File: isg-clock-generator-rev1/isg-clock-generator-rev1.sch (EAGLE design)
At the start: 160 parts, among them IC1 LMK03318RHSR, IC4 TPS7A8001DRBR, IC5 TPS7A8001DRBR, Q1 7M50072001, X1 OUT2_P, X2 OUT2_N, X3 OUT0_P, X4 PRIREF_P, X5 PRIREF_N, X6 V_IN_EXT

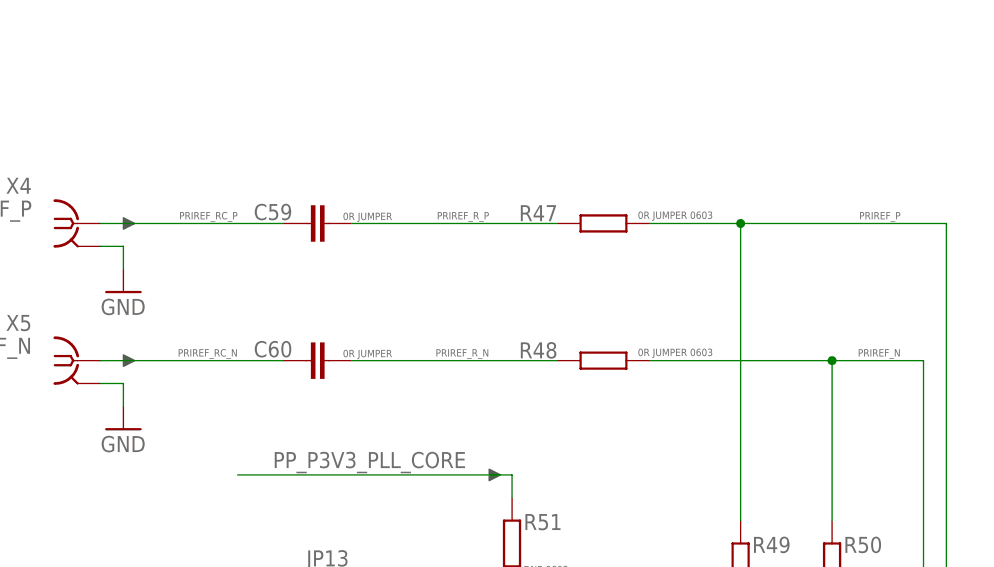
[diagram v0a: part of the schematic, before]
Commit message: Preliminary connections made to PRIREF inputs
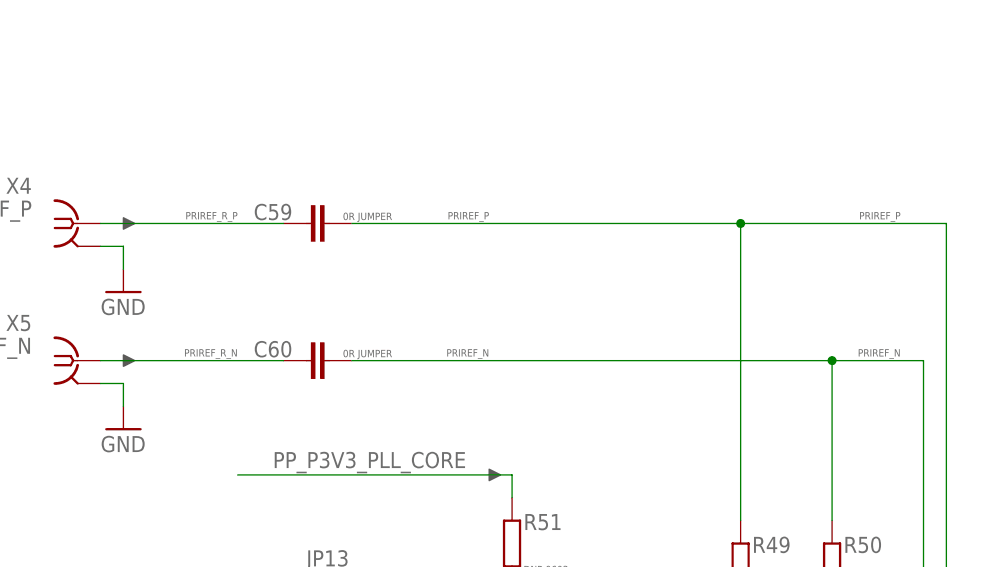
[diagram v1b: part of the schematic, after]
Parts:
- removed R47, R48: 0R JUMPER 0603, rcl-modified-footprints:R-EU_R0603
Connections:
- removed net PRIREF_RC_N: C60.1, X5.1
- removed net PRIREF_RC_P: C59.1, X4.1
- net PRIREF_N: now also C60.2; no longer R48.1
- net PRIREF_P: now also C59.2; no longer R47.1
- net PRIREF_R_N: now also C60.1, X5.1; no longer C60.2, R48.2
- net PRIREF_R_P: now also C59.1, X4.1; no longer C59.2, R47.2
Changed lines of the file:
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@@
 <part name="GND80" library="supply1" library_urn="urn:adsk.eagle:library:371" deviceset="GND" device=""/>
 <part name="GND81" library="supply1" library_urn="urn:adsk.eagle:library:371" deviceset="GND" device=""/>
-<part name="R47" library="rcl-modified-footprints" deviceset="R-EU_" device="R0603" package3d_urn="urn:adsk.eagle:package:23555/2" value="0R JUMPER 0603"/>
-<part name="R48" library="rcl-modified-footprints" deviceset="R-EU_" device="R0603" package3d_urn="urn:adsk.eagle:package:23555/2" value="0R JUMPER 0603"/>
 <part name="C59" library="rcl-modified-footprints" deviceset="C-EU" device="C0603" package3d_urn="urn:adsk.eagle:package:23616/2" value="0R JUMPER"/>
 <part name="C60" library="rcl-modified-footprints" deviceset="C-EU" device="C0603" package3d_urn="urn:adsk.eagle:package:23616/2" value="0R JUMPER"/>
@@
 <attribute name="VALUE" x="43.18" y="231.14" size="1.778" layer="96"/>
 </instance>
-<instance part="R47" gate="G$1" x="99.06" y="256.54" smashed="yes" rot="R180">
-<attribute name="NAME" x="93.98" y="258.572" size="1.778" layer="95" rot="R180"/>
-<attribute name="VALUE" x="102.87" y="257.048" size="0.8128" layer="96"/>
-</instance>
-<instance part="R48" gate="G$1" x="99.06" y="241.3" smashed="yes" rot="R180">
-<attribute name="NAME" x="93.98" y="243.332" size="1.778" layer="95" rot="R180"/>
-<attribute name="VALUE" x="102.87" y="241.808" size="0.8128" layer="96"/>
-</instance>
 <instance part="C59" gate="G$1" x="66.04" y="256.54" smashed="yes" rot="R90">
 <attribute name="NAME" x="64.516" y="258.699" size="1.778" layer="95" rot="R180"/>
@@
 <wire x1="134.62" y1="165.1" x2="134.62" y2="241.3" width="0.1524" layer="91"/>
 <wire x1="134.62" y1="241.3" x2="124.46" y2="241.3" width="0.1524" layer="91"/>
-<pinref part="R48" gate="G$1" pin="1"/>
 <pinref part="R50" gate="G$1" pin="2"/>
-<wire x1="124.46" y1="241.3" x2="104.14" y2="241.3" width="0.1524" layer="91"/>
 <wire x1="124.46" y1="223.52" x2="124.46" y2="241.3" width="0.1524" layer="91"/>
 <junction x="124.46" y="241.3"/>
 <label x="312.42" y="166.37" size="0.8128" layer="95" rot="R180"/>
 <label x="132.08" y="242.57" size="0.8128" layer="95" rot="R180"/>
-</segment>
-</net>
-<net name="PRIREF_P" class="0">
-<segment>
-<pinref part="IC1" gate="A" pin="PRIREF_P"/>
-<wire x1="314.96" y1="167.64" x2="137.16" y2="167.64" width="0.1524" layer="91"/>
-<wire x1="137.16" y1="167.64" x2="137.16" y2="256.54" width="0.1524" layer="91"/>
-<pinref part="R47" gate="G$1" pin="1"/>
-<wire x1="137.16" y1="256.54" x2="114.3" y2="256.54" width="0.1524" layer="91"/>
-<pinref part="R49" gate="G$1" pin="2"/>
-<wire x1="114.3" y1="256.54" x2="104.14" y2="256.54" width="0.1524" layer="91"/>
-<wire x1="114.3" y1="223.52" x2="114.3" y2="256.54" width="0.1524" layer="91"/>
-<junction x="114.3" y="256.54"/>
-<label x="312.42" y="168.91" size="0.8128" layer="95" rot="R180"/>
-<label x="132.08" y="257.81" size="0.8128" layer="95" rot="R180"/>
+<pinref part="C60" gate="G$1" pin="2"/>
+<wire x1="124.46" y1="241.3" x2="71.12" y2="241.3" width="0.1524" layer="91"/>
+<label x="86.36" y="242.57" size="0.8128" layer="95" rot="R180"/>
 </segment>
 </net>
@@
 </segment>
 </net>
-<net name="PRIREF_RC_P" class="0">
+<net name="PRIREF_R_P" class="0">
 <segment>
 <pinref part="X4" gate="G1" pin="1"/>
@@
 </segment>
 </net>
-<net name="PRIREF_R_P" class="0">
-<segment>
-<pinref part="C59" gate="G$1" pin="2"/>
-<pinref part="R47" gate="G$1" pin="2"/>
-<wire x1="71.12" y1="256.54" x2="93.98" y2="256.54" width="0.1524" layer="91"/>
-<label x="86.36" y="257.81" size="0.8128" layer="95" rot="R180"/>
-</segment>
-</net>
 <net name="PRIREF_R_N" class="0">
 <segment>
-<pinref part="R48" gate="G$1" pin="2"/>
-<pinref part="C60" gate="G$1" pin="2"/>
-<wire x1="93.98" y1="241.3" x2="71.12" y2="241.3" width="0.1524" layer="91"/>
-<label x="86.36" y="242.57" size="0.8128" layer="95" rot="R180"/>
-</segment>
-</net>
-<net name="PRIREF_RC_N" class="0">
-<segment>
 <pinref part="C60" gate="G$1" pin="1"/>
 <pinref part="X5" gate="G1" pin="1"/>
@@
 </segment>
 </net>
+<net name="PRIREF_P" class="0">
+<segment>
+<pinref part="C59" gate="G$1" pin="2"/>
+<wire x1="71.12" y1="256.54" x2="114.3" y2="256.54" width="0.1524" layer="91"/>
+<label x="86.36" y="257.81" size="0.8128" layer="95" rot="R180"/>
+<pinref part="IC1" gate="A" pin="PRIREF_P"/>
+<wire x1="314.96" y1="167.64" x2="137.16" y2="167.64" width="0.1524" layer="91"/>
+<wire x1="137.16" y1="167.64" x2="137.16" y2="256.54" width="0.1524" layer="91"/>
+<wire x1="137.16" y1="256.54" x2="114.3" y2="256.54" width="0.1524" layer="91"/>
+<pinref part="R49" gate="G$1" pin="2"/>
+<wire x1="114.3" y1="223.52" x2="114.3" y2="256.54" width="0.1524" layer="91"/>
+<junction x="114.3" y="256.54"/>
+<label x="312.42" y="168.91" size="0.8128" layer="95" rot="R180"/>
+<label x="132.08" y="257.81" size="0.8128" layer="95" rot="R180"/>
+</segment>
+</net>

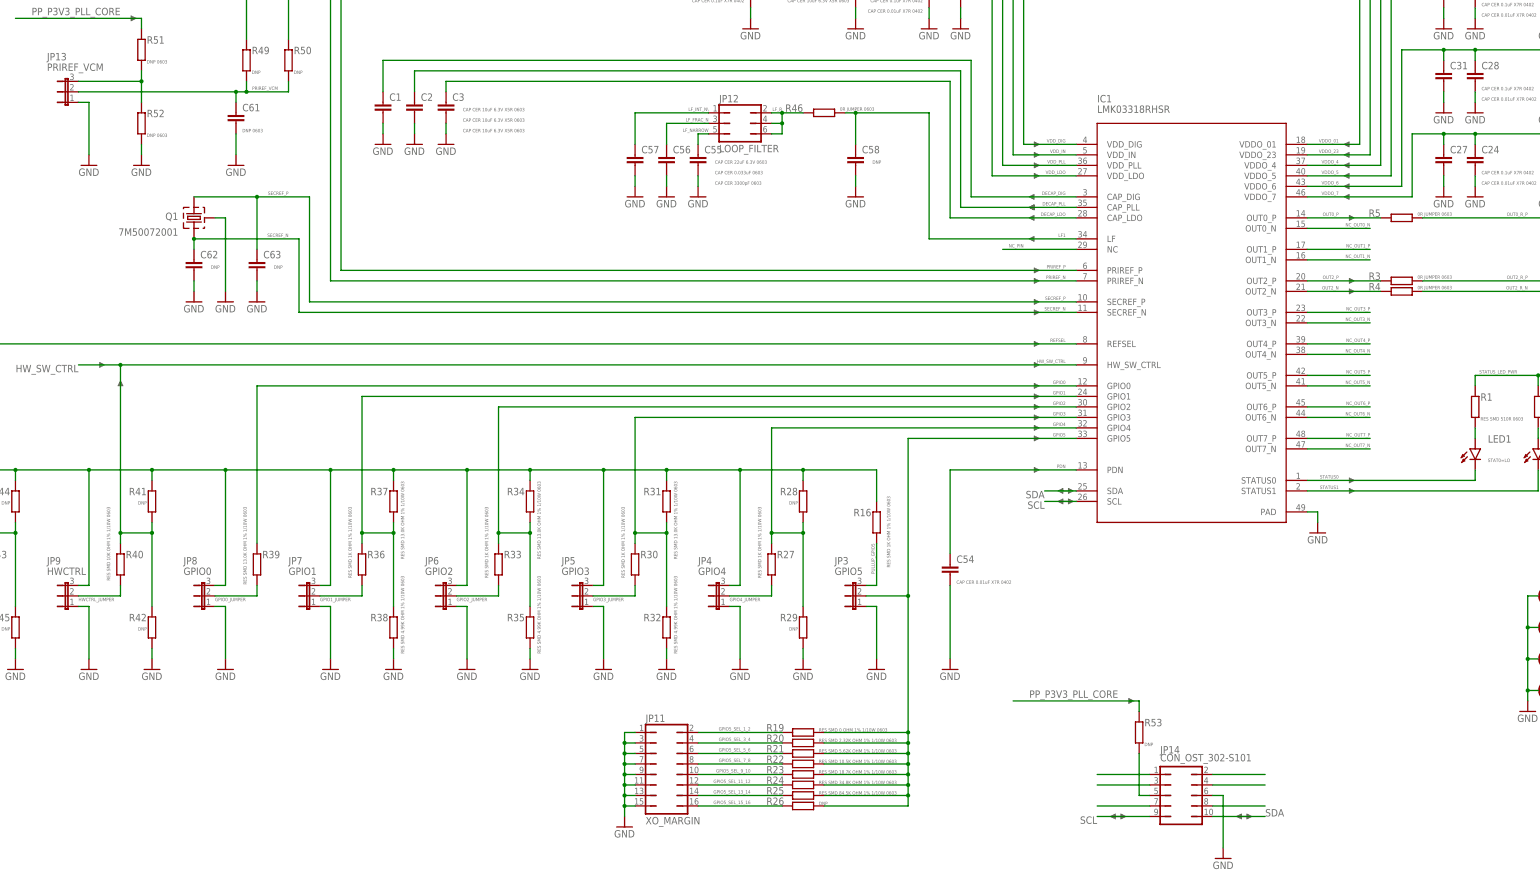
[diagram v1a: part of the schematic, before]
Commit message: Close to done, VIN still unconnected and TPS needs package fixed
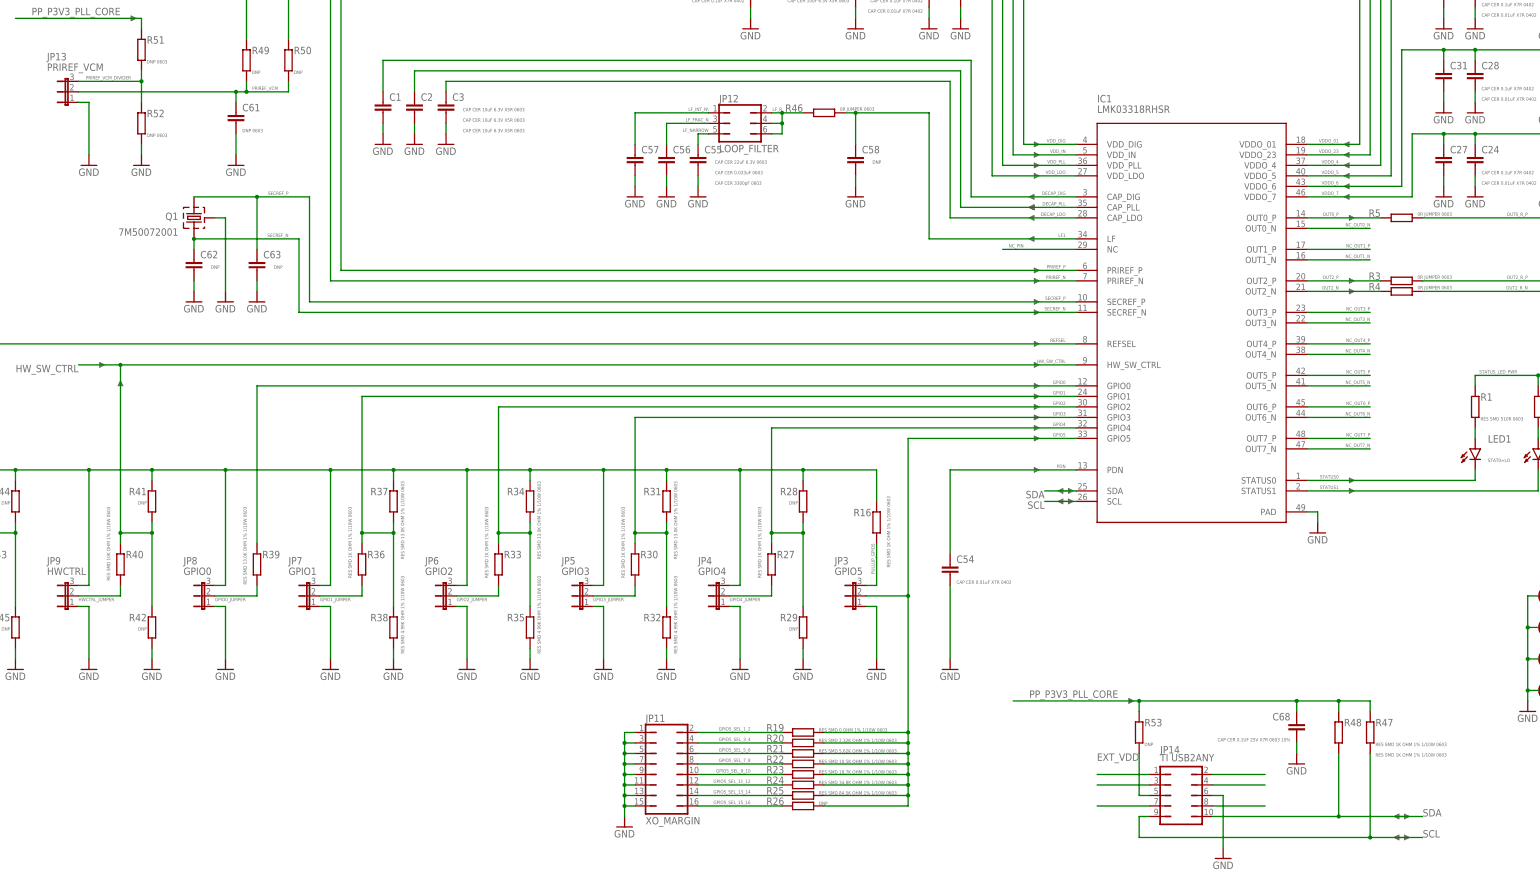
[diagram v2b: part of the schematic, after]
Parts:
- added C68: CAP CER 0.1UF 25V X7R 0603 10%, rcl-modified-footprints:C-EUC0603
- added R47, R48: RES SMD 1K OHM 1% 1/10W 0603, rcl-modified-footprints:R-EU_R0603
- JP14: value CON_OST_302-S101 -> TI USB2ANY
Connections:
- net N$5 renamed PRIREF_VCM_DIVIDER
- net N$6 renamed EXT_VDD
- net GND: now also C68.2
- net PP_P3V3_PLL_CORE: now also C68.1, R47.2, R48.2
- net SCL: now also R47.1
- net SDA: now also R48.1
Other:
- note added: "OST 302-S101"
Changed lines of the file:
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@@
 <part name="DNP49" library="meng" deviceset="ARROW_1DIR" device=""/>
 <part name="GND78" library="supply1" library_urn="urn:adsk.eagle:library:371" deviceset="GND" device=""/>
-<part name="JP14" library="Kramnik's Library" deviceset="CON_OST_302-S101" device=""/>
+<part name="JP14" library="Kramnik's Library" deviceset="CON_OST_302-S101" device="" value="TI USB2ANY"/>
 <part name="R51" library="rcl-modified-footprints" deviceset="R-EU_" device="R0603" package3d_urn="urn:adsk.eagle:package:23555/2" value="DNP 0603"/>
 <part name="R52" library="rcl-modified-footprints" deviceset="R-EU_" device="R0603" package3d_urn="urn:adsk.eagle:package:23555/2" value="DNP 0603"/>
@@
 <part name="GND91" library="supply1" library_urn="urn:adsk.eagle:library:371" deviceset="GND" device=""/>
 <part name="GND92" library="supply1" library_urn="urn:adsk.eagle:library:371" deviceset="GND" device=""/>
+<part name="R47" library="rcl-modified-footprints" deviceset="R-EU_" device="R0603" package3d_urn="urn:adsk.eagle:package:23555/2" value="RES SMD 1K OHM 1% 1/10W 0603"/>
+<part name="R48" library="rcl-modified-footprints" deviceset="R-EU_" device="R0603" package3d_urn="urn:adsk.eagle:package:23555/2" value="RES SMD 1K OHM 1% 1/10W 0603"/>
+<part name="C68" library="rcl-modified-footprints" deviceset="C-EU" device="C0603" package3d_urn="urn:adsk.eagle:package:23616/2" value="CAP CER 0.1UF 25V X7R 0603 10%"/>
+<part name="GND93" library="supply1" library_urn="urn:adsk.eagle:library:371" deviceset="GND" device=""/>
 </parts>
 <sheets>
@@
 <text x="403.86" y="170.18" size="1.778" layer="98">1.8V^2 / 50R = 64.8mW = 1/16W
 (so std. 0402 49.9R resistor can't be burnt out under any conditions)</text>
+<text x="335.28" y="17.78" size="1.778" layer="98">OST 302-S101</text>
 </plain>
 <instances>
@@
 <instance part="DNP51" gate="G$1" x="45.72" y="241.3" smashed="yes"/>
 <instance part="DNP52" gate="G$1" x="45.72" y="256.54" smashed="yes"/>
-<instance part="DNP53" gate="G$1" x="325.12" y="35.56" smashed="yes"/>
-<instance part="DNP54" gate="G$1" x="355.6" y="35.56" smashed="yes"/>
+<instance part="DNP53" gate="G$1" x="393.7" y="30.48" smashed="yes"/>
+<instance part="DNP54" gate="G$1" x="393.7" y="35.56" smashed="yes"/>
 <instance part="DNP55" gate="G$1" x="312.42" y="114.3" smashed="yes"/>
 <instance part="DNP56" gate="G$1" x="312.42" y="111.76" smashed="yes"/>
@@
 <instance part="GND92" gate="1" x="109.22" y="160.02" smashed="yes">
 <attribute name="VALUE" x="106.68" y="157.48" size="1.778" layer="96"/>
+</instance>
+<instance part="R47" gate="G$1" x="386.08" y="55.88" smashed="yes" rot="R90">
+<attribute name="NAME" x="387.35" y="57.3786" size="1.778" layer="95"/>
+<attribute name="VALUE" x="387.35" y="52.578" size="0.8128" layer="96"/>
+</instance>
+<instance part="R48" gate="G$1" x="378.46" y="55.88" smashed="yes" rot="R90">
+<attribute name="NAME" x="379.73" y="57.3786" size="1.778" layer="95"/>
+<attribute name="VALUE" x="387.35" y="50.038" size="0.8128" layer="96"/>
+</instance>
+<instance part="C68" gate="G$1" x="368.3" y="58.42" smashed="yes" rot="MR0">
+<attribute name="NAME" x="366.776" y="58.801" size="1.778" layer="95" rot="MR0"/>
+<attribute name="VALUE" x="366.776" y="53.721" size="0.8128" layer="96" rot="MR0"/>
+</instance>
+<instance part="GND93" gate="1" x="368.3" y="48.26" smashed="yes">
+<attribute name="VALUE" x="365.76" y="45.72" size="1.778" layer="96"/>
 </instance>
 </instances>
@@
 <wire x1="109.22" y1="180.34" x2="106.68" y2="180.34" width="0.1524" layer="91"/>
 </segment>
+<segment>
+<pinref part="GND93" gate="1" pin="GND"/>
+<pinref part="C68" gate="G$1" pin="2"/>
+<wire x1="368.3" y1="50.8" x2="368.3" y2="53.34" width="0.1524" layer="91"/>
+</segment>
 </net>
 <net name="DECAP_LDO" class="0">
@@
 <segment>
 <pinref part="JP14" gate="G$1" pin="10"/>
-<wire x1="347.98" y1="35.56" x2="360.68" y2="35.56" width="0.1524" layer="91"/>
-<label x="360.68" y="35.56" size="1.778" layer="95"/>
+<wire x1="347.98" y1="35.56" x2="378.46" y2="35.56" width="0.1524" layer="91"/>
+<label x="398.78" y="35.56" size="1.778" layer="95"/>
+<pinref part="R48" gate="G$1" pin="1"/>
+<wire x1="378.46" y1="35.56" x2="398.78" y2="35.56" width="0.1524" layer="91"/>
+<wire x1="378.46" y1="50.8" x2="378.46" y2="35.56" width="0.1524" layer="91"/>
+<junction x="378.46" y="35.56"/>
 </segment>
 <segment>
@@
 <segment>
 <pinref part="JP14" gate="G$1" pin="9"/>
-<wire x1="332.74" y1="35.56" x2="320.04" y2="35.56" width="0.1524" layer="91"/>
-<label x="320.04" y="35.56" size="1.778" layer="95" rot="R180"/>
+<wire x1="332.74" y1="35.56" x2="330.2" y2="35.56" width="0.1524" layer="91"/>
+<label x="398.78" y="30.48" size="1.778" layer="95"/>
+<wire x1="330.2" y1="35.56" x2="330.2" y2="30.48" width="0.1524" layer="91"/>
+<wire x1="330.2" y1="30.48" x2="386.08" y2="30.48" width="0.1524" layer="91"/>
+<pinref part="R47" gate="G$1" pin="1"/>
+<wire x1="386.08" y1="30.48" x2="398.78" y2="30.48" width="0.1524" layer="91"/>
+<wire x1="386.08" y1="50.8" x2="386.08" y2="30.48" width="0.1524" layer="91"/>
+<junction x="386.08" y="30.48"/>
 </segment>
 <segment>
@@
 <wire x1="330.2" y1="63.5" x2="299.72" y2="63.5" width="0.1524" layer="91"/>
 <label x="325.12" y="66.04" size="1.778" layer="95" rot="R180"/>
+<pinref part="C68" gate="G$1" pin="1"/>
+<wire x1="330.2" y1="63.5" x2="368.3" y2="63.5" width="0.1524" layer="91"/>
+<wire x1="368.3" y1="63.5" x2="368.3" y2="60.96" width="0.1524" layer="91"/>
+<junction x="330.2" y="63.5"/>
+<wire x1="368.3" y1="63.5" x2="378.46" y2="63.5" width="0.1524" layer="91"/>
+<junction x="368.3" y="63.5"/>
+<pinref part="R48" gate="G$1" pin="2"/>
+<wire x1="378.46" y1="63.5" x2="378.46" y2="60.96" width="0.1524" layer="91"/>
+<wire x1="378.46" y1="63.5" x2="386.08" y2="63.5" width="0.1524" layer="91"/>
+<junction x="378.46" y="63.5"/>
+<pinref part="R47" gate="G$1" pin="2"/>
+<wire x1="386.08" y1="63.5" x2="386.08" y2="60.96" width="0.1524" layer="91"/>
 </segment>
 </net>
@@
 </segment>
 </net>
-<net name="N$5" class="0">
+<net name="PRIREF_VCM_DIVIDER" class="0">
 <segment>
 <pinref part="JP13" gate="1" pin="3"/>
@@
 <wire x1="88.9" y1="213.36" x2="88.9" y2="208.28" width="0.1524" layer="91"/>
 <junction x="88.9" y="213.36"/>
-</segment>
-</net>
-<net name="N$6" class="0">
+<label x="86.36" y="214.63" size="0.8128" layer="95" rot="R180"/>
+</segment>
+</net>
+<net name="EXT_VDD" class="0">
 <segment>
 <pinref part="JP14" gate="G$1" pin="5"/>
@@
 <wire x1="330.2" y1="40.64" x2="330.2" y2="50.8" width="0.1524" layer="91"/>
 <pinref part="R53" gate="G$1" pin="1"/>
-</segment>
-</net>
+<label x="330.2" y="50.8" size="1.778" layer="95" rot="R180"/>
+</segment>
+</net>

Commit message: Fixed TPS landing pattern
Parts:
- added R54: 0R JUMPER 0603, rcl-modified-footprints:R-EU_R0603
- C50, C52, C64: value 0R JUMPER -> 0R JUMPER 0402
- JP1: value MOTHERBOARD -> EOS_MOTHERBOARD
- JP14: value TI USB2ANY -> TI_USB2ANY
- R3, R4, R5: value 0R JUMPER 0603 -> 0R JUMPER 0402
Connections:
- new net GPIO5_JUMPER: JP3.2, R19.1, R20.1, R21.1, R22.1, R23.1, R24.1, R25.1, R26.1, R54.2
- net GPIO5: now also R54.1; no longer JP3.2, R19.1, R20.1, R21.1, R22.1, R23.1, R24.1, R25.1, R26.1
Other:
- note added: "0.0 V"
- note added: "0.2 V"
- note added: "0.4 V"
- note added: "0.6 V"
- note added: "0.8 V"
- note added: "1.0 V"
- note added: "1.2 V"
- note added: "1.4 V"
